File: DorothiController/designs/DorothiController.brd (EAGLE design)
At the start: 76.2 x 30.5 mm, 25 parts

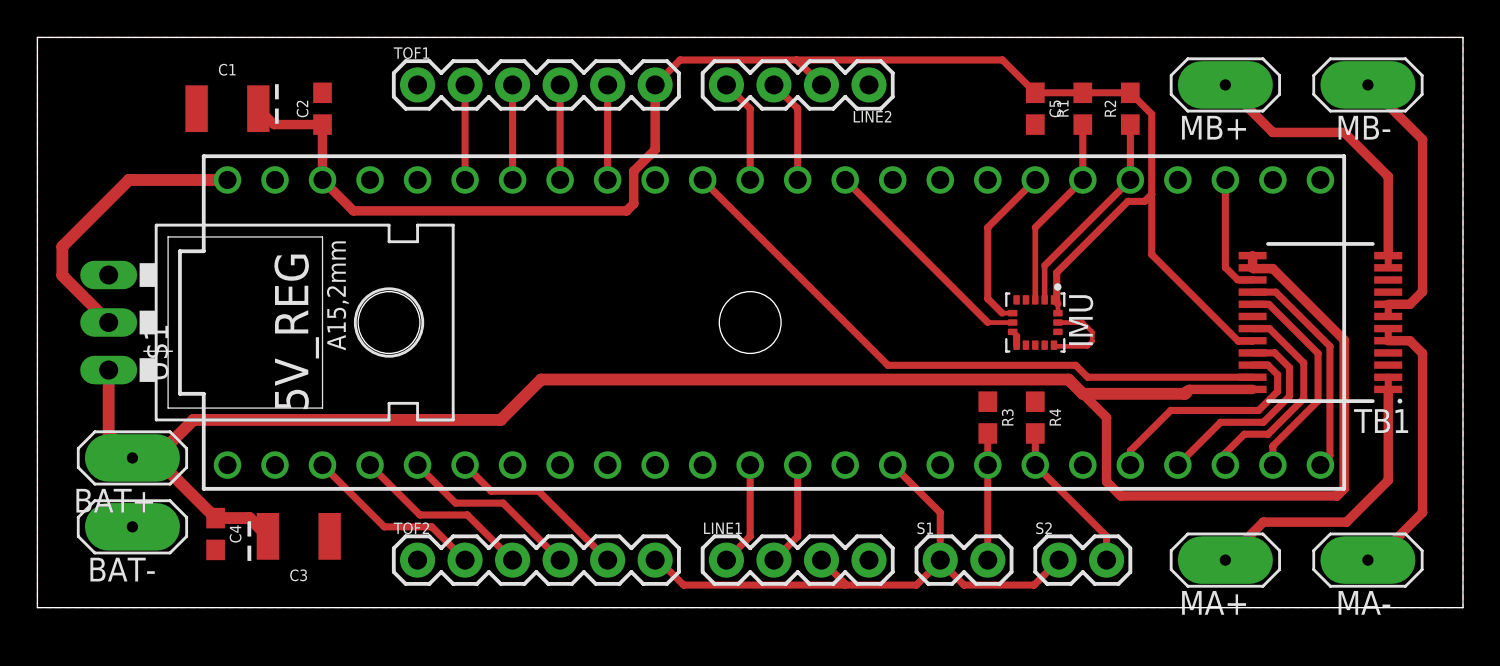
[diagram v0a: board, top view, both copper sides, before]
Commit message: silk screen and status diode added
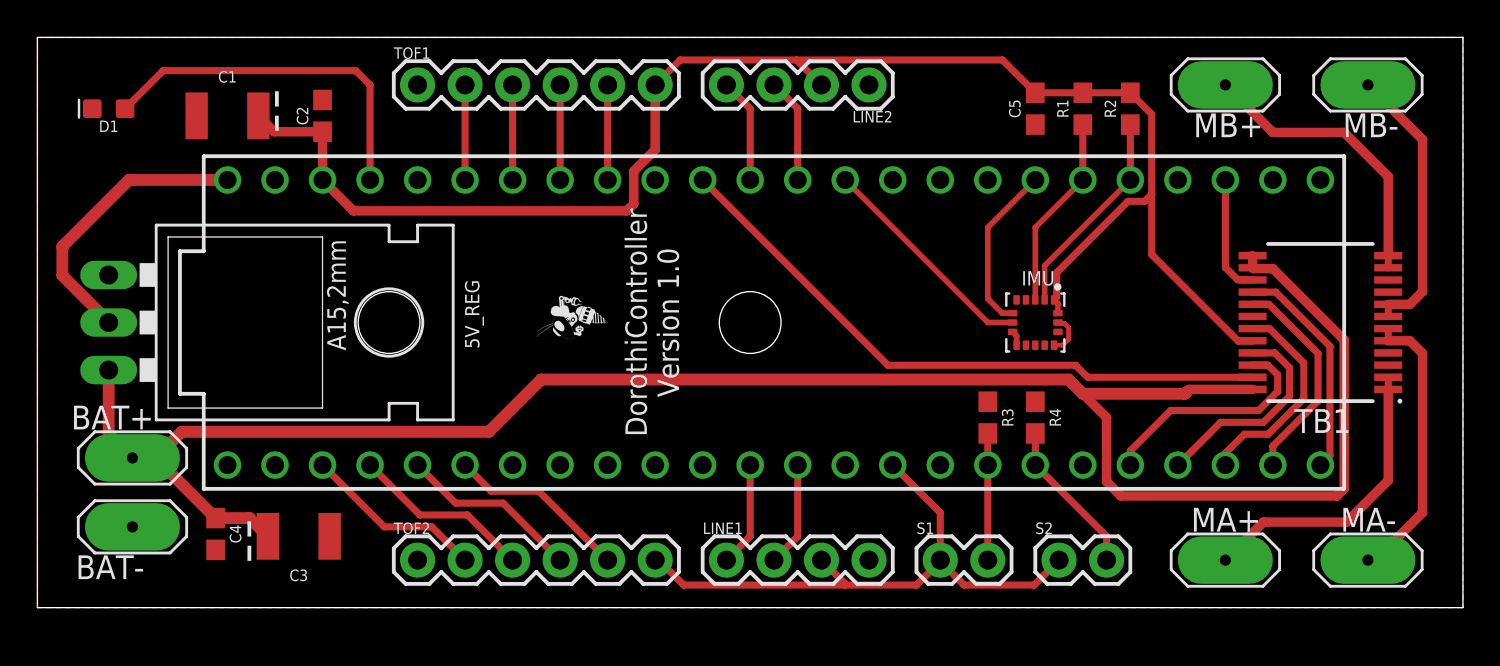
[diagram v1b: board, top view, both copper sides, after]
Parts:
- added D1: (no value), SparkFun-LED:LED-0603
- added U$2: ROBOBUZZ0.2X, RoboJackets-Aesthetics:ROBOBUZZ_0.2X
- moved C1 0.38 mm to (10.2, 26.3)
- moved C2 0.38 mm to (15.2, 26.3)
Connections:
- new net INDICATOR: D1.A, U$1.23/A9
- net GND: now also D1.C
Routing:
- net INDICATOR: track 0.00 -> 19.3 mm
- net GND: track 5.53 -> 3.01 mm
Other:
- board text added: "DorothiController Version 1.0"

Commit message: forgot resistor
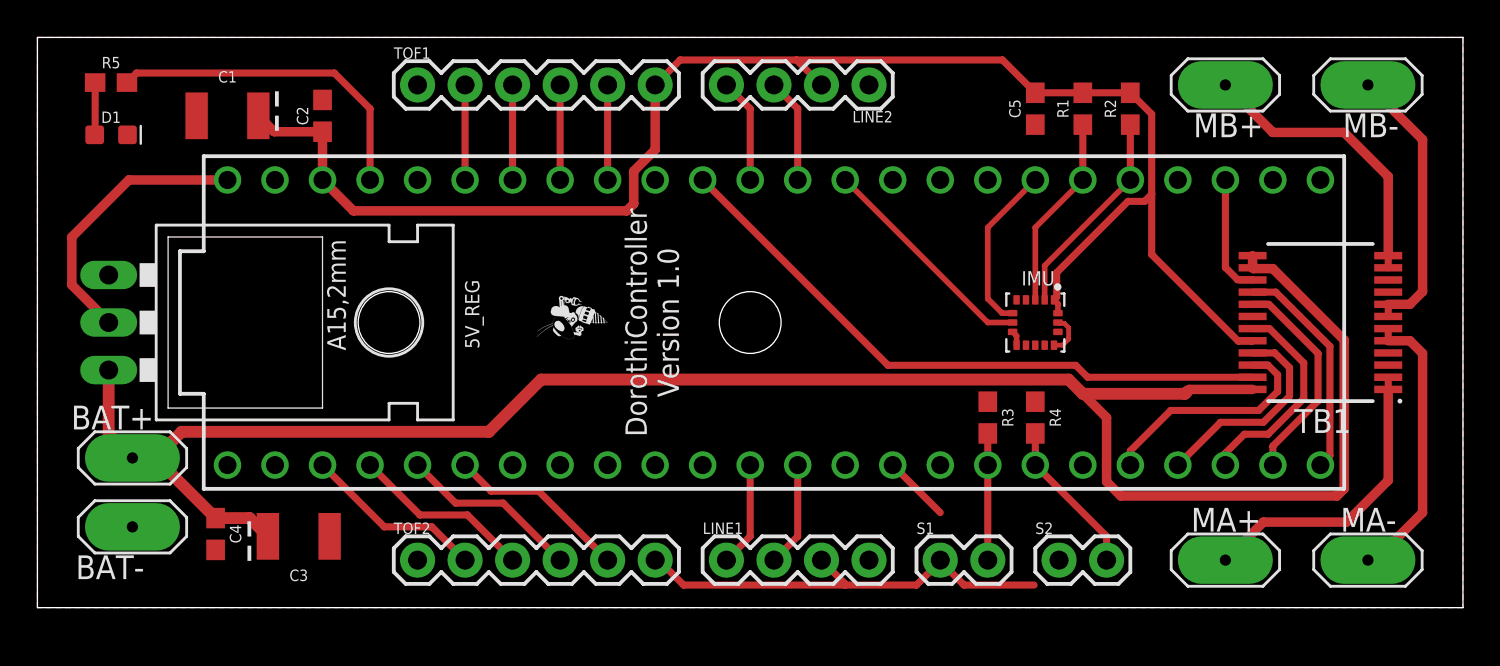
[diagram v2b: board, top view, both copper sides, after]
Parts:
- added R5: 10k, SparkFun-Resistors:0603
- moved D1 1.40 mm to (3.94, 25.3), turned to 0 degrees
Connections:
- new net N$5: D1.A, R5.1
- net INDICATOR: now also R5.2; no longer D1.A
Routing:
- net +3V3: track 116.6 -> 112.1 mm
- net N$5: track 0.00 -> 2.81 mm
- net INDICATOR: track 19.3 -> 17.8 mm
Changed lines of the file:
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@@
 <attribute name="VALUE" x="8.763" y="3.937" size="0.6096" layer="27" font="vector" ratio="20" rot="R270" align="top-center"/>
 </element>
-<element name="D1" library="SparkFun-LED" library_urn="urn:adsk.eagle:library:529" package="LED-0603" package3d_urn="urn:adsk.eagle:package:39354/1" value="" x="3.81" y="26.67" smashed="yes" rot="R180">
-<attribute name="NAME" x="3.81" y="26.035" size="0.6096" layer="25" font="vector" ratio="20" rot="R180" align="bottom-center"/>
-<attribute name="VALUE" x="3.81" y="27.305" size="0.6096" layer="27" font="vector" ratio="20" rot="R180" align="top-center"/>
+<element name="D1" library="SparkFun-LED" library_urn="urn:adsk.eagle:library:529" package="LED-0603" package3d_urn="urn:adsk.eagle:package:39354/1" value="" x="3.937" y="25.273" smashed="yes">
+<attribute name="NAME" x="3.937" y="25.908" size="0.6096" layer="25" font="vector" ratio="20" align="bottom-center"/>
+<attribute name="VALUE" x="3.937" y="24.638" size="0.6096" layer="27" font="vector" ratio="20" align="top-center"/>
 </element>
 <element name="U$2" library="RoboJackets-Aesthetics" package="ROBOBUZZ_0.2X" value="ROBOBUZZ0.2X" x="30.48" y="15.24" smashed="yes" rot="R90"/>
+<element name="R5" library="SparkFun-Resistors" library_urn="urn:adsk.eagle:library:532" package="0603" package3d_urn="urn:adsk.eagle:package:39650/1" value="10k" x="3.937" y="28.067" smashed="yes">
+<attribute name="NAME" x="3.937" y="28.829" size="0.6096" layer="25" font="vector" ratio="20" align="bottom-center"/>
+<attribute name="PROD_ID" value="RES-00824" x="3.937" y="28.067" size="1.778" layer="27" display="off"/>
+<attribute name="VALUE" x="3.937" y="27.305" size="0.6096" layer="27" font="vector" ratio="20" align="top-center"/>
+</element>
 </elements>
 <signals>
@@
 <contactref element="R2" pad="2"/>
 <contactref element="LINE2" pad="2"/>
-<contactref element="S1" pad="1"/>
-<contactref element="S2" pad="1"/>
 <contactref element="TB1" pad="20"/>
 <contactref element="C1" pad="A"/>
 <contactref element="C2" pad="1"/>
 <contactref element="LINE1" pad="3"/>
-<wire x1="48.26" y1="2.54" x2="48.26" y2="5.08" width="0.381" layer="1"/>
 <wire x1="48.26" y1="5.08" x2="45.72" y2="7.62" width="0.381" layer="1"/>
-<wire x1="54.61" y1="2.54" x2="53.2765" y2="1.2065" width="0.381" layer="1"/>
 <wire x1="53.2765" y1="1.2065" x2="49.53" y2="1.2065" width="0.381" layer="1"/>
 <wire x1="49.53" y1="1.2065" x2="48.26" y2="2.4765" width="0.381" layer="1"/>
-<wire x1="48.26" y1="2.4765" x2="48.26" y2="2.54" width="0.381" layer="1"/>
 <wire x1="15.24" y1="22.86" x2="16.891" y2="21.209" width="0.508" layer="1"/>
 <wire x1="16.891" y1="21.209" x2="31.496" y2="21.209" width="0.508" layer="1"/>
@@
 <wire x1="54.34" y1="16.45" x2="54.483" y2="16.593" width="0.3302" layer="1"/>
 <wire x1="54.483" y1="16.593" x2="54.483" y2="17.907" width="0.381" layer="1"/>
-<wire x1="45.72" y1="7.62" x2="54.55" y2="15.74" width="0" layer="19" extent="1-1"/>
+<contactref element="S1" pad="1"/>
+<contactref element="S2" pad="1"/>
+<wire x1="53.2765" y1="1.2065" x2="54.61" y2="2.54" width="0" layer="19" extent="1-1"/>
+<wire x1="48.26" y1="2.54" x2="48.26" y2="2.4765" width="0" layer="19" extent="1-1"/>
+<wire x1="48.26" y1="5.08" x2="48.26" y2="2.54" width="0" layer="19" extent="1-1"/>
+<wire x1="54.55" y1="15.74" x2="45.72" y2="7.62" width="0" layer="19" extent="1-1"/>
 </signal>
 <signal name="5V_OUT">
@@
 <contactref element="U$1" pad="VIN"/>
 <wire x1="3.81" y1="15.24" x2="3.81" y2="15.275825" width="0.635" layer="1"/>
-<wire x1="3.81" y1="15.275825" x2="1.3335" y2="17.752325" width="0.635" layer="1"/>
-<wire x1="1.3335" y1="17.752325" x2="1.3335" y2="19.304" width="0.635" layer="1"/>
-<wire x1="1.3335" y1="19.304" x2="4.8895" y2="22.86" width="0.635" layer="1"/>
-<wire x1="4.8895" y1="22.86" x2="10.16" y2="22.86" width="0.635" layer="1"/>
+<wire x1="3.81" y1="15.275825" x2="1.8415" y2="17.244325" width="0.508" layer="1"/>
+<wire x1="1.8415" y1="17.244325" x2="1.8415" y2="19.812" width="0.508" layer="1"/>
+<wire x1="1.8415" y1="19.812" x2="4.8895" y2="22.86" width="0.508" layer="1"/>
+<wire x1="4.8895" y1="22.86" x2="10.16" y2="22.86" width="0.508" layer="1"/>
 </signal>
 <signal name="+12V">
@@
 <wire x1="72.205" y1="15.565" x2="72.205" y2="16.215" width="0.381" layer="1"/>
 </signal>
+<signal name="N$5">
+<contactref element="R5" pad="1"/>
+<contactref element="D1" pad="A"/>
+<wire x1="3.087" y1="28.067" x2="3.087" y2="25.3" width="0.381" layer="1"/>
+<wire x1="3.087" y1="25.3" x2="3.06" y2="25.273" width="0.381" layer="1"/>
+</signal>
 <signal name="INDICATOR">
 <contactref element="U$1" pad="23/A9"/>
-<contactref element="D1" pad="A"/>
-<wire x1="17.78" y1="22.86" x2="17.78" y2="27.94" width="0.381" layer="1"/>
-<wire x1="17.78" y1="27.94" x2="17.018" y2="28.702" width="0.381" layer="1"/>
-<wire x1="6.719" y1="28.702" x2="4.687" y2="26.67" width="0.381" layer="1"/>
-<wire x1="17.018" y1="28.702" x2="6.719" y2="28.702" width="0.381" layer="1"/>
+<contactref element="R5" pad="2"/>
+<wire x1="17.78" y1="22.86" x2="17.78" y2="26.67" width="0.381" layer="1"/>
+<wire x1="17.78" y1="26.67" x2="15.875" y2="28.575" width="0.381" layer="1"/>
+<wire x1="5.295" y1="28.575" x2="4.787" y2="28.067" width="0.381" layer="1"/>
+<wire x1="15.875" y1="28.575" x2="5.295" y2="28.575" width="0.381" layer="1"/>
 </signal>
 </signals>
